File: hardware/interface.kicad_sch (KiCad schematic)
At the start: 0 parts

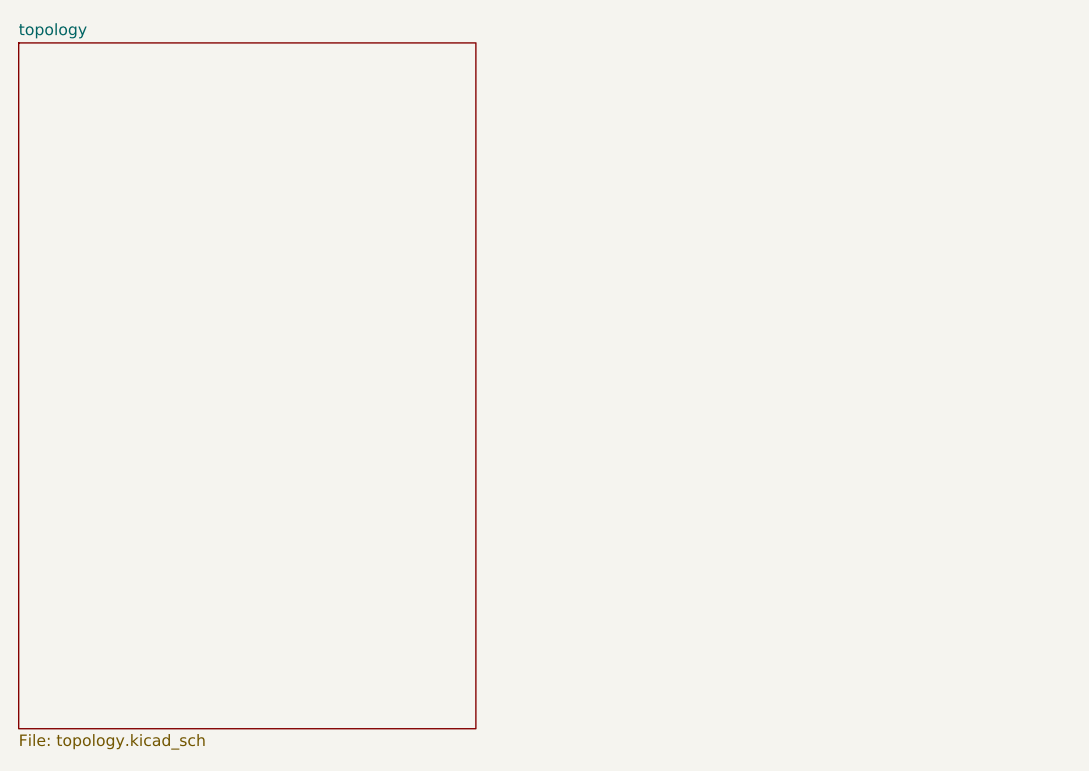
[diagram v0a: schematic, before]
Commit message: Hardware: Updated Schematics and inicial ESP32 schematic
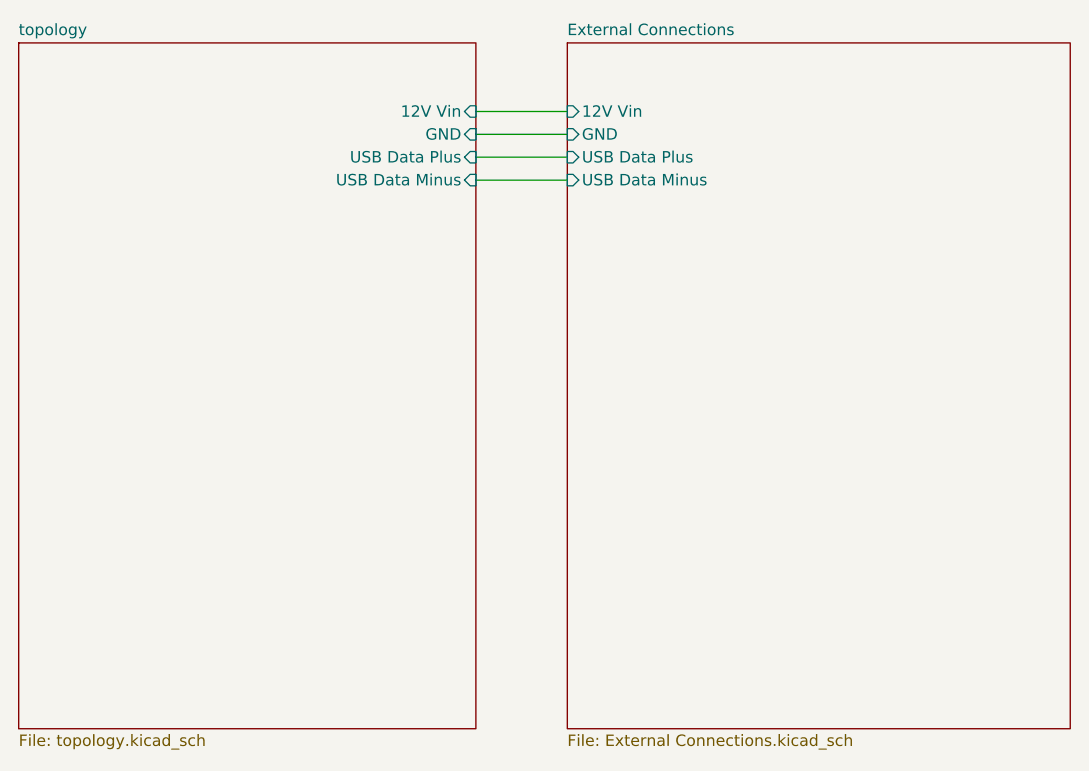
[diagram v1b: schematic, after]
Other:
- added sheet External Connections (External Connections.kicad_sch)
- sheet topology ports: added 12V Vin, GND, USB Data Minus, USB Data Plus; removed none
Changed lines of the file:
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@@
 	(generator_version "9.0")
 	(paper "A4")
+	(wire
+		(pts
+			(xy 81.28 43.18) (xy 91.44 43.18)
+		)
+		(stroke
+			(width 0)
+			(type default)
+		)
+	)
+	(wire
+		(pts
+			(xy 81.28 50.8) (xy 91.44 50.8)
+		)
+		(stroke
+			(width 0)
+			(type default)
+		)
+	)
+	(wire
+		(pts
+			(xy 81.28 48.26) (xy 91.44 48.26)
+		)
+		(stroke
+			(width 0)
+			(type default)
+		)
+	)
+	(wire
+		(pts
+			(xy 81.28 45.72) (xy 91.44 45.72)
+		)
+		(stroke
+			(width 0)
+			(type default)
+		)
+	)
 	(sheet
 		(at 30.48 35.56)
@@
 			)
 		)
+		(pin "12V Vin" input
+			(at 81.28 43.18 0)
+			(effects
+				(font
+					(size 1.27 1.27)
+				)
+				(justify right)
+			)
+		)
+		(pin "GND" input
+			(at 81.28 45.72 0)
+			(effects
+				(font
+					(size 1.27 1.27)
+				)
+				(justify right)
+			)
+		)
+		(pin "USB Data Minus" input
+			(at 81.28 50.8 0)
+			(effects
+				(font
+					(size 1.27 1.27)
+				)
+				(justify right)
+			)
+		)
+		(pin "USB Data Plus" input
+			(at 81.28 48.26 0)
+			(effects
+				(font
+					(size 1.27 1.27)
+				)
+				(justify right)
+			)
+		)
 		(instances
 			(project "RelogioGRS"
@@
 				)
 			)
+		)
+	)
+	(sheet
+		(at 91.44 35.56)
+		(size 55.88 76.2)
+		(exclude_from_sim no)
+		(in_bom yes)
+		(on_board yes)
+		(dnp no)
+		(fields_autoplaced yes)
+		(stroke
+			(width 0.1524)
+			(type solid)
+		)
+		(fill
+			(color 0 0 0 0.0000)
+		)
+		(property "Sheetname" "External Connections"
+			(at 91.44 34.8484 0)
+			(effects
+				(font
+					(size 1.27 1.27)
+				)
+				(justify left bottom)
+			)
+		)
+		(property "Sheetfile" "External Connections.kicad_sch"
+			(at 91.44 112.3446 0)
+			(effects
+				(font
+					(size 1.27 1.27)
+				)
+				(justify left top)
+			)
+		)
+		(pin "12V Vin" input
+			(at 91.44 43.18 180)
+			(effects
+				(font
+					(size 1.27 1.27)
+				)
+				(justify left)
+			)
+		)
+		(pin "GND" input
+			(at 91.44 45.72 180)
+			(effects
+				(font
+					(size 1.27 1.27)
+				)
+				(justify left)
+			)
+		)
+		(pin "USB Data Minus" input
+			(at 91.44 50.8 180)
+			(effects
+				(font
+					(size 1.27 1.27)
+				)
+				(justify left)
+			)
+		)
+		(pin "USB Data Plus" input
+			(at 91.44 48.26 180)
+			(effects
+				(font
+					(size 1.27 1.27)
+				)
+				(justify left)
+			)
+		)
+		(instances
+			(project "RelogioGRS"
+				(path "/c5089fae-3fc0-463b-a1cd-29d25b5e00c5/88c473a8-a79d-4818-8d16-2e360f67bb0b"
+					(page "9")
+				)
+			)
